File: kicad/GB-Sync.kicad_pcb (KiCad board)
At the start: 2 copper layers, 18.3 x 18.3 mm, 5 parts

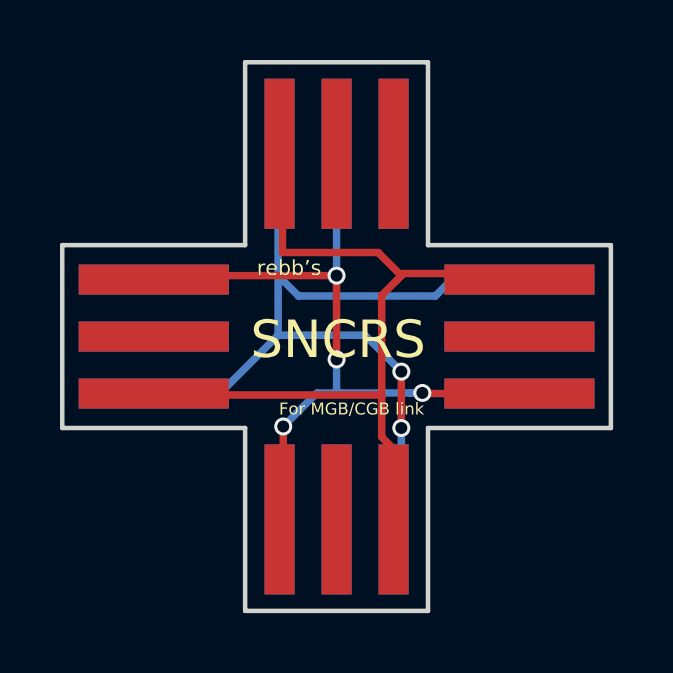
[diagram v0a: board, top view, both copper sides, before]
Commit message: Added some marks to indicate link cable facing and master/lead port
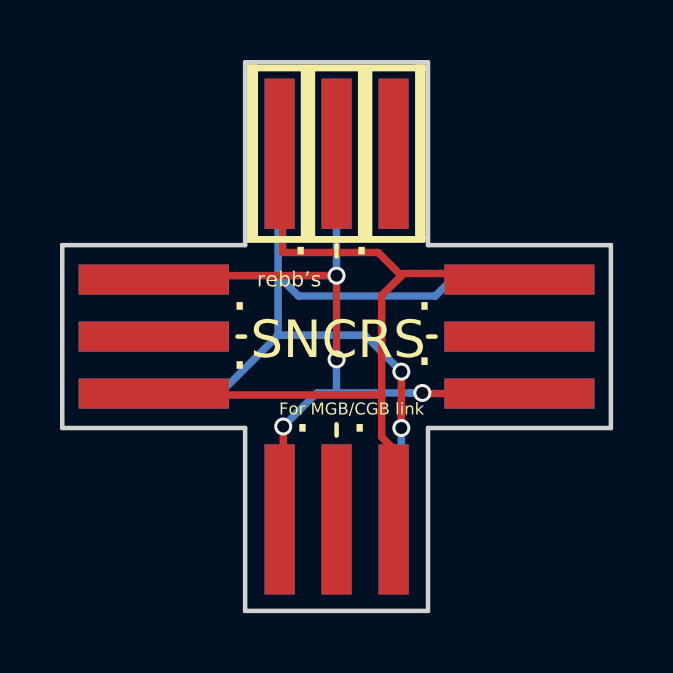
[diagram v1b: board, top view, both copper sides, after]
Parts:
- removed G***: LOGO, gb_link:twinpeaks
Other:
- board text added: "."
- board text added: "2020/04"
- board text removed: "2018/10"
